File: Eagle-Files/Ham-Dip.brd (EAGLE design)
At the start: 41.1 x 50 mm, 14 parts, among them IC1 MAX232ECWE

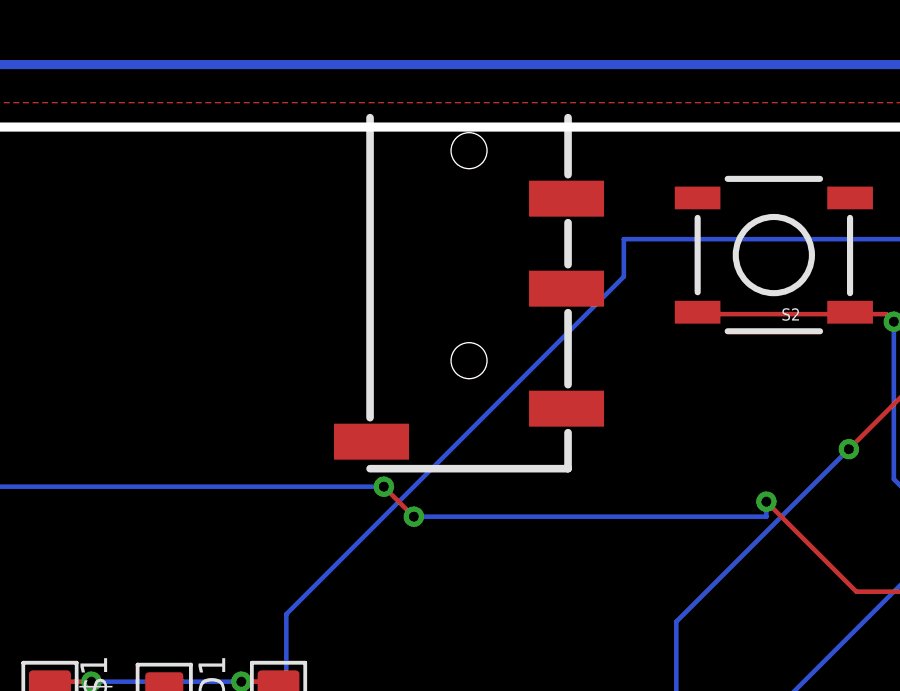
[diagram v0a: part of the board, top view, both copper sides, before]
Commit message: Corrected Wiring on TRRS Jack
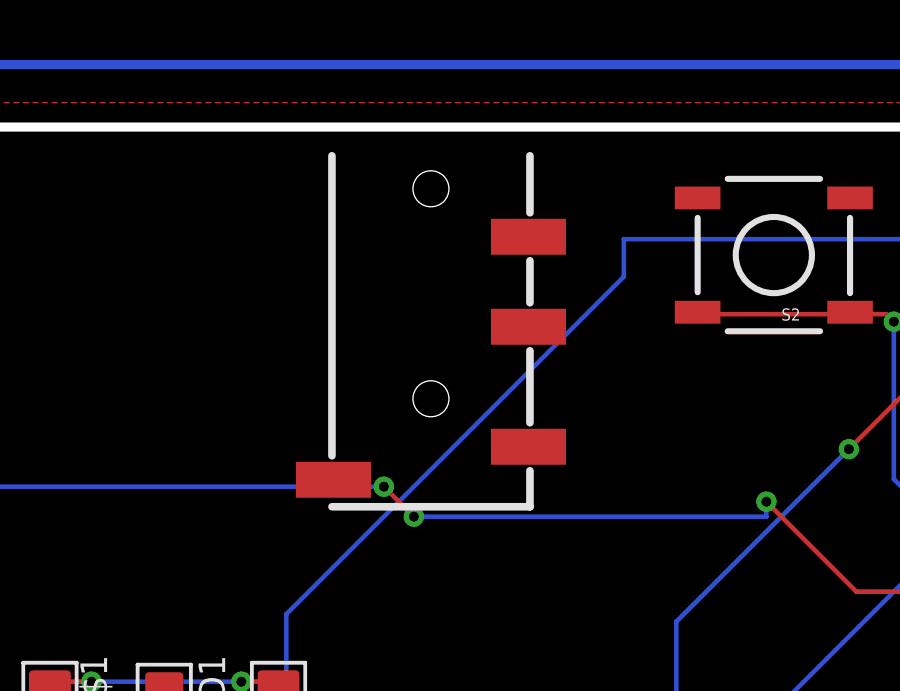
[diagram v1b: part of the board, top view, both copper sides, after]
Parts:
- moved TRRS 1.80 mm to (20.3, 49.5)
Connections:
- net SPARE renamed GPIO-#
- net CW-KEY-1: now also TRRS.TIP; no longer TRRS.RING1
- net CW-KEY-2: now also TRRS.RING1; no longer TRRS.TIP
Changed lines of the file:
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@@
 <attribute name="MPN" value="RC0805JR-07220RL" x="15.24" y="30.48" size="1.778" layer="27" rot="R180" display="off"/>
 </element>
-<element name="TRRS" library="SparkFun-Connectors" package="AUDIO-JACK-TRRS-SMD" value="AUDIO-JACK3" x="21.59" y="50.8" rot="R270"/>
+<element name="TRRS" library="SparkFun-Connectors" package="AUDIO-JACK-TRRS-SMD" value="AUDIO-JACK3" x="20.32" y="49.53" rot="R270"/>
 </elements>
 <signals>
@@
 <signal name="CW-KEY-1">
 <contactref element="U$2" pad="57"/>
-<contactref element="TRRS" pad="RING1"/>
-<wire x1="37.01" y1="26.81" x2="24.84" y2="44.6" width="0" layer="19" extent="1-1"/>
+<contactref element="TRRS" pad="TIP"/>
+<wire x1="23.57" y1="39.33" x2="37.01" y2="26.81" width="0" layer="19" extent="1-1"/>
 </signal>
 <signal name="CW-KEY-2">
 <contactref element="U$2" pad="55"/>
-<contactref element="TRRS" pad="TIP"/>
-<wire x1="37.01" y1="24.27" x2="24.84" y2="40.6" width="0" layer="19" extent="1-1"/>
+<contactref element="TRRS" pad="RING1"/>
+<wire x1="37.01" y1="24.27" x2="23.57" y2="43.33" width="0" layer="19" extent="1-1"/>
 </signal>
 <signal name="FEL">
@@
 <wire x1="15" y1="29.75" x2="15.24" y2="29.591" width="0.1524" layer="1"/>
 </signal>
-<signal name="SPARE">
+<signal name="GPIO-#">
 <contactref element="TRRS" pad="RING2"/>
 </signal>
